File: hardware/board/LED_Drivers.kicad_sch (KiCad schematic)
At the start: 73 parts, among them Q901 MMBT3906

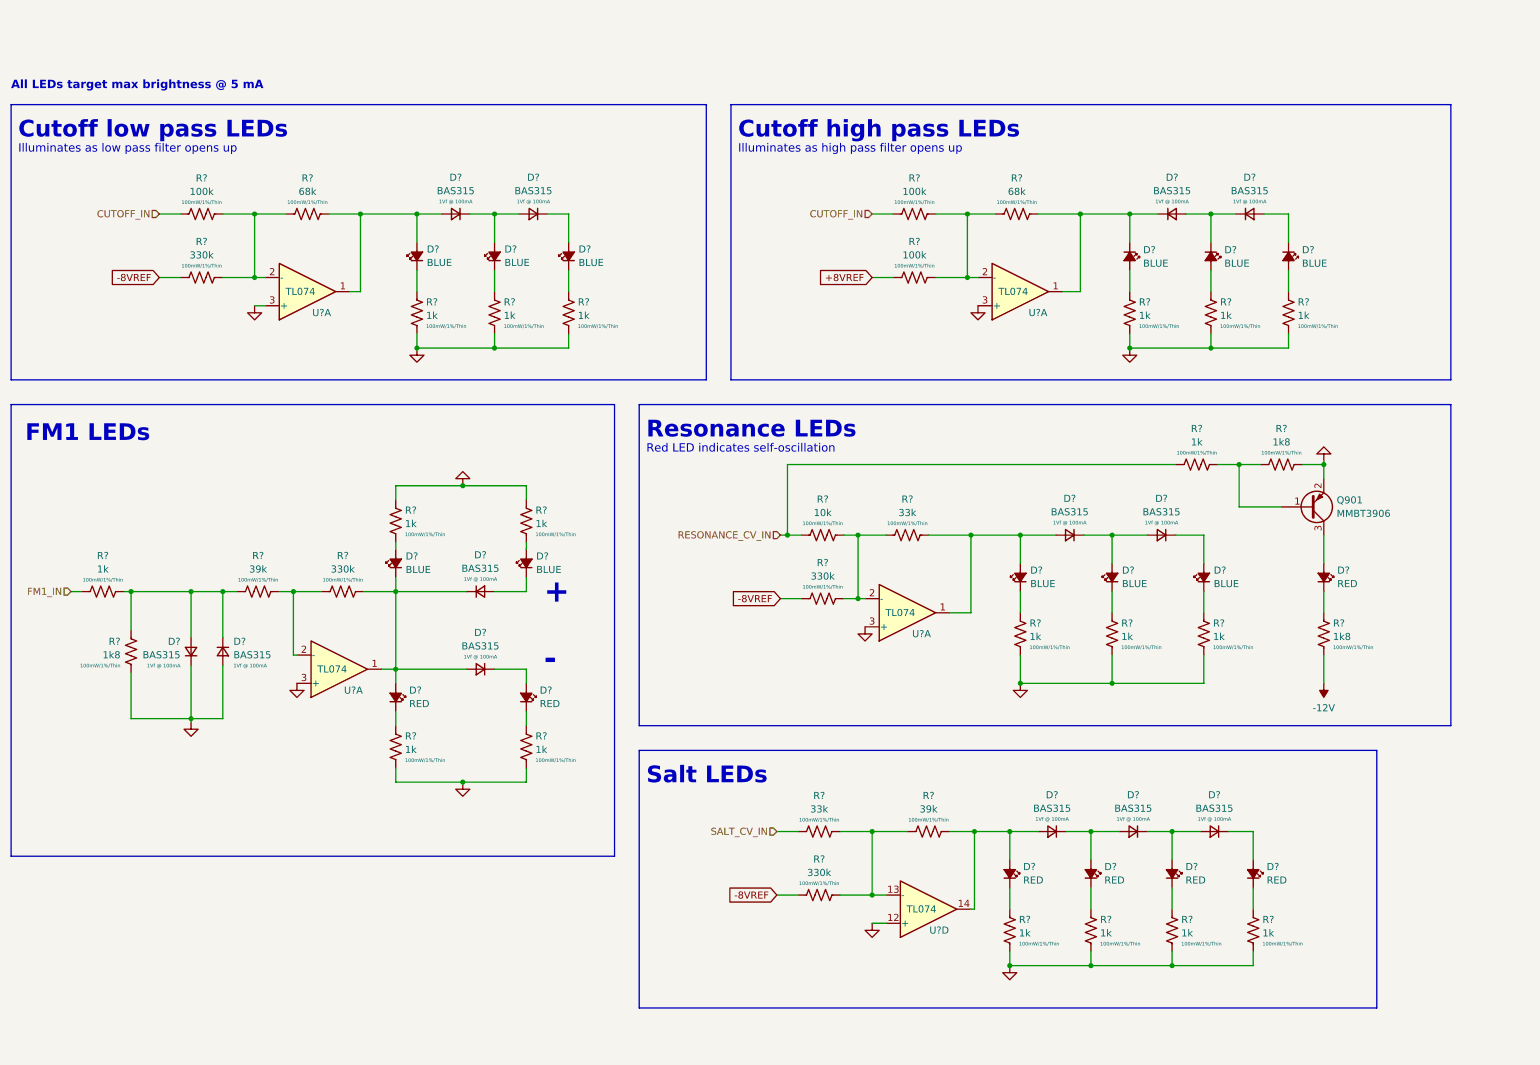
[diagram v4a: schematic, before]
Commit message: hardware: finalize v3
- Updated version number and release date
- Swapped TL074C to TL074H
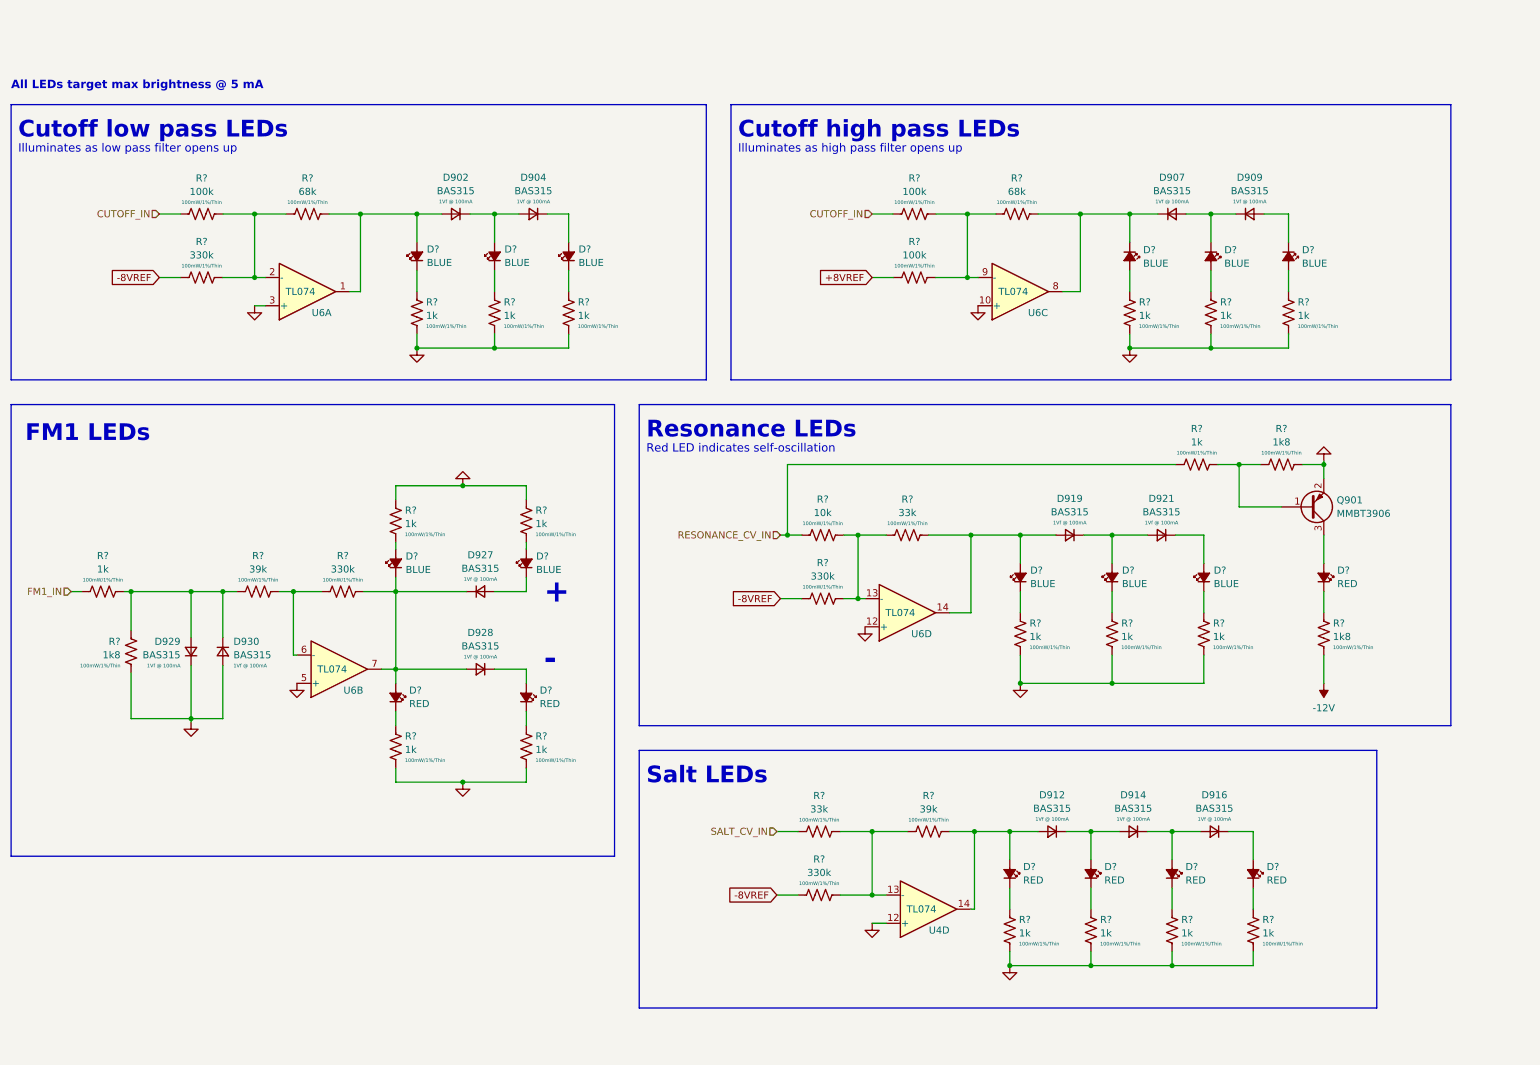
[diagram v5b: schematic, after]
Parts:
- U4, U6: renamed from U?; DigiKey 296-7198-1-ND -> 296-TL074HIPWRCT-ND; LCSC C96507 -> C4370424; MPN TL074CPWR -> TL074HIPWR; Notes (none) -> TL074H over TL074C due to better input offset voltage
- gave numbers to parts that had none: 13
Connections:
- net GND: now also U6.10 (+), U6.12 (+), U6.5 (+); no longer U6.3 (+), U6.3 (+), U6.3 (+)
- net at D927.1 (K), D928.2 (A), D?.1 (K)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: now also U6.7; no longer U6.1
- net at D919.2 (A), D?.2 (A), R?.1: now also U6.14; no longer U6.1
- net at D907.1 (K), D?.1 (K), R?.2: now also U6.8; no longer U6.1
- net at R?.2, R?.2: now also U6.6 (-); no longer U6.2 (-)
- net at R?.1, R?.1, R?.1: now also U6.9 (-); no longer U6.2 (-)
- net at R?.1, R?.1, R?.2: now also U6.13 (-); no longer U6.2 (-)
